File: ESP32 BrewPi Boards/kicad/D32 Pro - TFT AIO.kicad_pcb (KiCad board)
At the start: 2 copper layers, 44 x 78 mm, 33 parts, among them J1 POWER, J2 5V IN, J3 TFT, J4 RELAY, J5 LCD, J6 RJ45, J7 GLYCOL, J8 OW_VSEL, Q1 BSS123, Q2 BSS123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

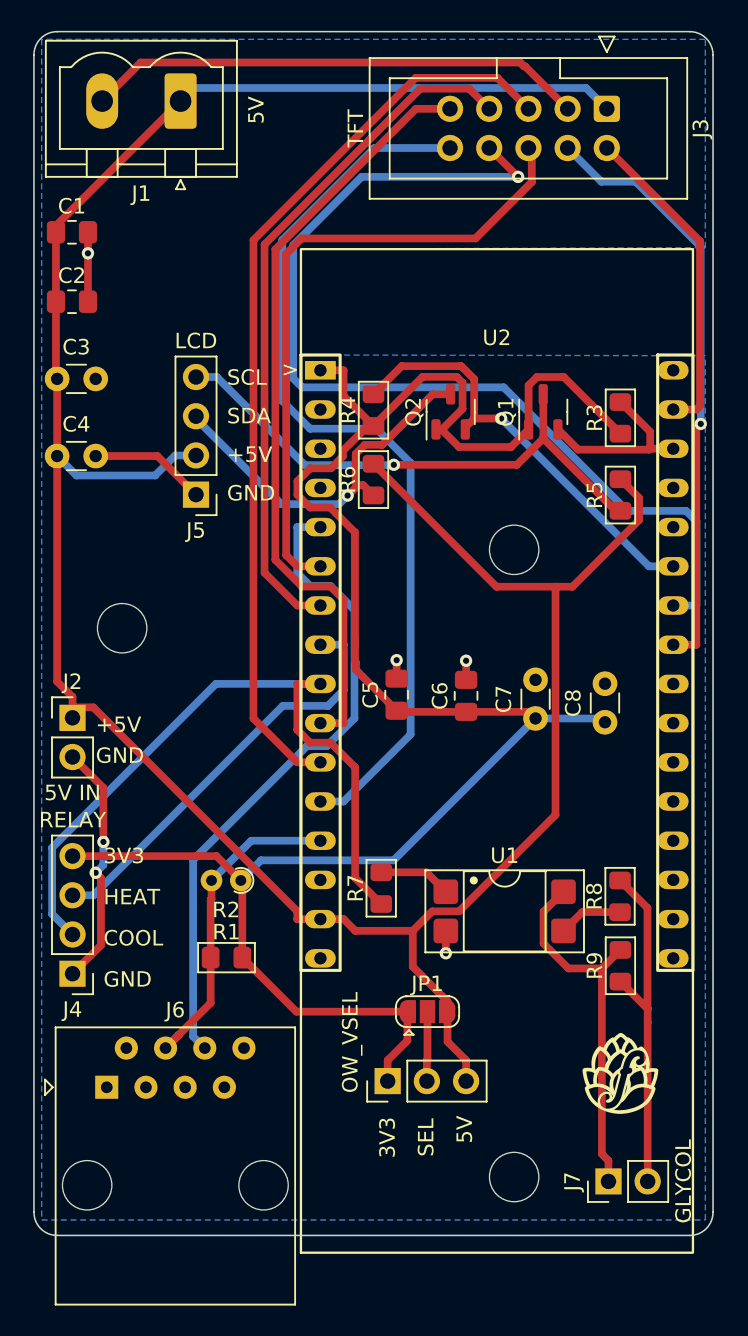
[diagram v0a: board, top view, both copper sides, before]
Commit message: Fix footprint for U1
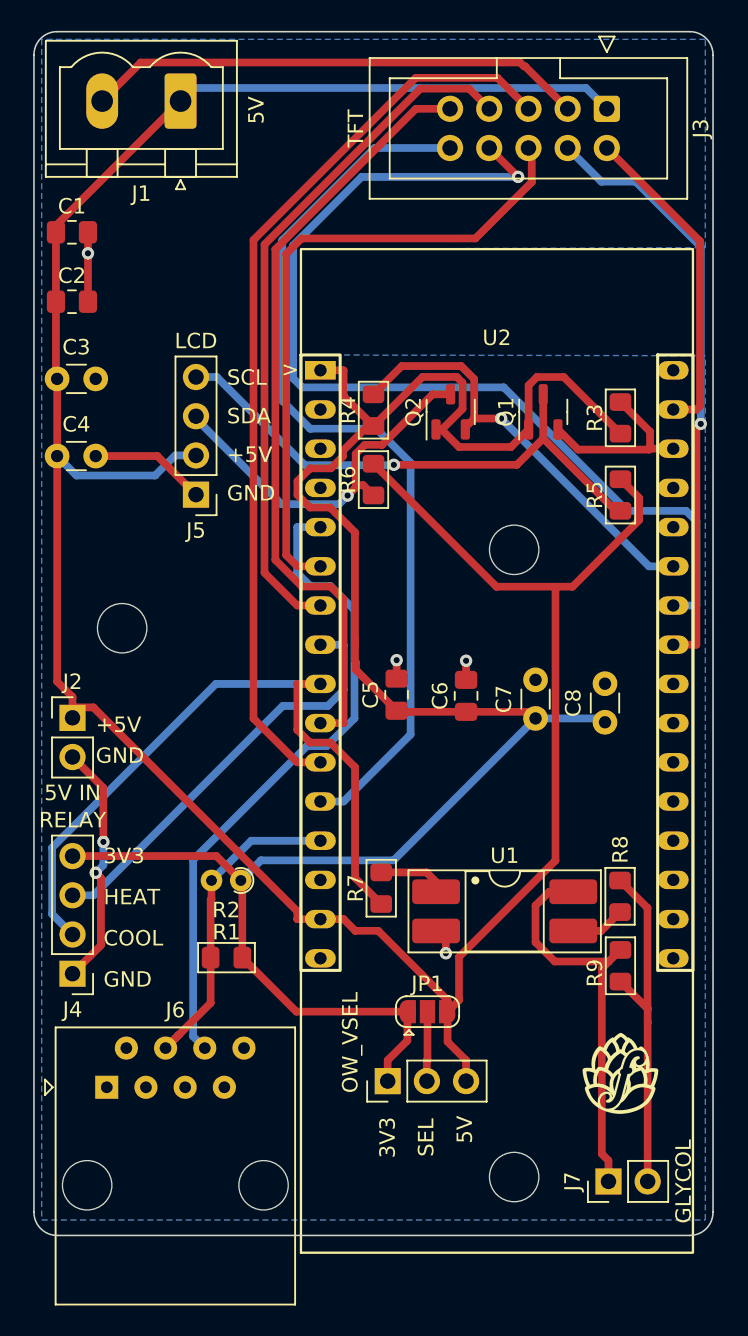
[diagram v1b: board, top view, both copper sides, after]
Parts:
- U1: footprint PCM_Package_DIP_AKL:DIP-4_W7.62mm_SMDSocket_SmallPads -> PCM_Package_DIP_AKL:DIP-4_W8.89mm_SMDSocket_LongPads
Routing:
- net Net-(J7-Pin_1): track 24.0 -> 26.1 mm
- net +5V: track 174.4 -> 176.4 mm
- net Net-(R8-Pad1): track 4.17 -> 3.54 mm

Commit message: Power to OneWire sensors
Add trace for power to onewire sensors, adjust silkscreen
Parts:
- added D1: IR26-21C_L110_TR8, LED_SMD:LED_0805_2012Metric_Pad1.15x1.40mm_HandSolder, F.Cu at (148.8, 45.4)
- added R10: 330R, Resistor_SMD:R_0805_2012Metric_Pad1.20x1.40mm_HandSolder, F.Cu at (148.8, 48.9)
- moved R6 21.2 mm to (139.3, 54.9), turned to 0 degrees
- moved Q2 19.0 mm to (141.3, 58.5)
- moved R4 14.9 mm to (143.8, 54.9), turned to 0 degrees
- moved R9 8.58 mm to (168.8, 93.4), turned to 180 degrees
- moved Q1 7.50 mm to (157.3, 66.0)
- moved R3 7.02 mm to (162.8, 65.9), turned to 0 degrees
- moved R8 6.54 mm to (168.9, 103.9), turned to 0 degrees
- moved R5 5.73 mm to (168.3, 65.9), turned to 0 degrees
- moved R7 3.54 mm to (154.8, 93.4), turned to 0 degrees
- moved J2 2.54 mm to (134.3, 88.4), turned to 180 degrees
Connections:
- J2 pad 1: +5V -> GND
- J2 pad 2: GND -> +5V
- J6 pad 3: unconnected-(J6-Pad3) -> Net-(J8-Pin_2)
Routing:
- net /SDA: track 28.0 -> 72.2 mm
- net GND: track 64.3 -> 99.2 mm, vias 6 -> 4
- net +3V3: track 130.1 -> 153.6 mm, vias 0 -> 1
- net Net-(J8-Pin_2): track 4.52 -> 26.9 mm
- net /5V_SDA: track 24.7 -> 15.9 mm, vias 1 -> 0
- net /5V_SCL: track 35.4 -> 29.8 mm
- net /COOL: track 46.7 -> 42.0 mm
- net /SCL: track 11.9 -> 16.5 mm, vias 0 -> 1
- net /MISO: track 64.6 -> 60.9 mm, vias 1 -> 0
- net Net-(D1-A): track 0.00 -> 3.52 mm
- net +5V: track 176.4 -> 178.3 mm
- net Net-(R8-Pad1): track 3.54 -> 5.15 mm
- net Net-(R7-Pad2): track 4.71 -> 5.78 mm
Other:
- board text added: "BrewPi D32 Pro AIO Board v0.2 @thorrak says hi Rev 20231125"
- board text removed: "BrewPi D32 Pro AIO Board v0.2 @thorrak says hi Rev 20231030"
